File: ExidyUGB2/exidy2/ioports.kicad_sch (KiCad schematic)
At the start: 65 parts, among them U10F_ 74LS04, U12H_ LM3900, U13H_ 74LS00, U14B 74LS374, U15A 74LS241, U15B 74LS245, U2C_ 74LS07, U6E_ 74LS112, U6F_ 74LS32, U7E_ 74LS139, U7F_ 74LS27, U8D 74LS374, U8E 74LS374, U8F_ 74LS02, U9D 74LS374, U9E 74LS241

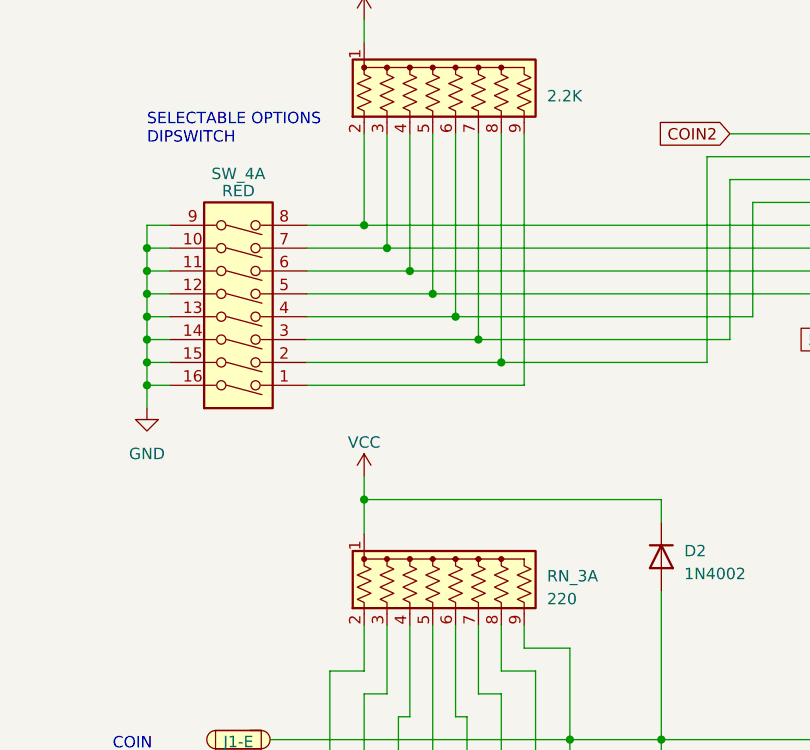
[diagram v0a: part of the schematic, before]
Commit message: Updates to KiCAD8
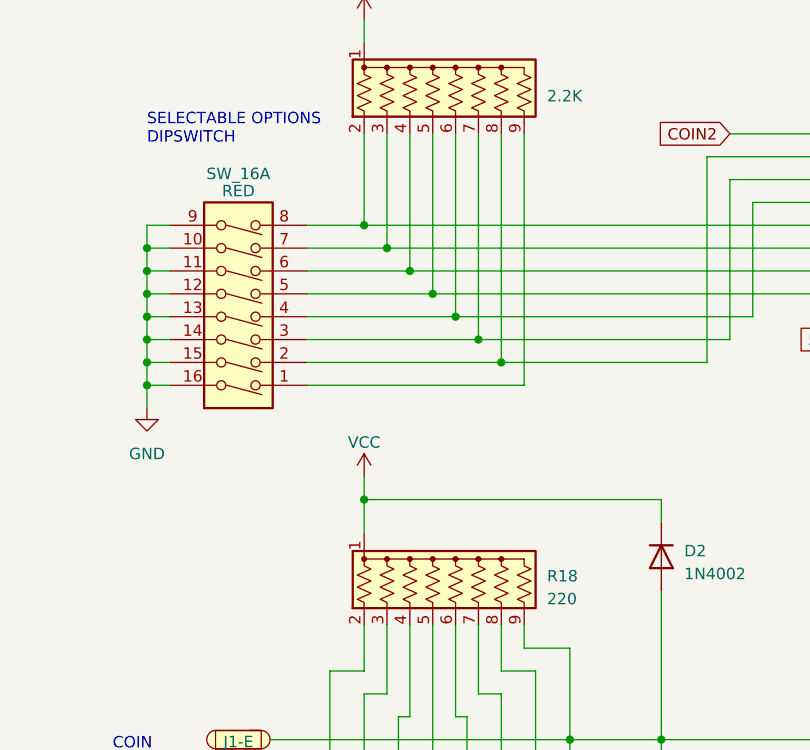
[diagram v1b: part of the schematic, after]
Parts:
- renumbered RN_3A to R18, RN_3A to RN?, SW_4A to SW_16A
